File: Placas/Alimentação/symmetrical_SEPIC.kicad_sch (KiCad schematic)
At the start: 10 parts, among them J13 Conn_01x01_Pin, J14 Conn_01x01_Pin, J15 Conn_01x01_Pin, J16 Conn_01x01_Pin, J17 Conn_01x01_Pin

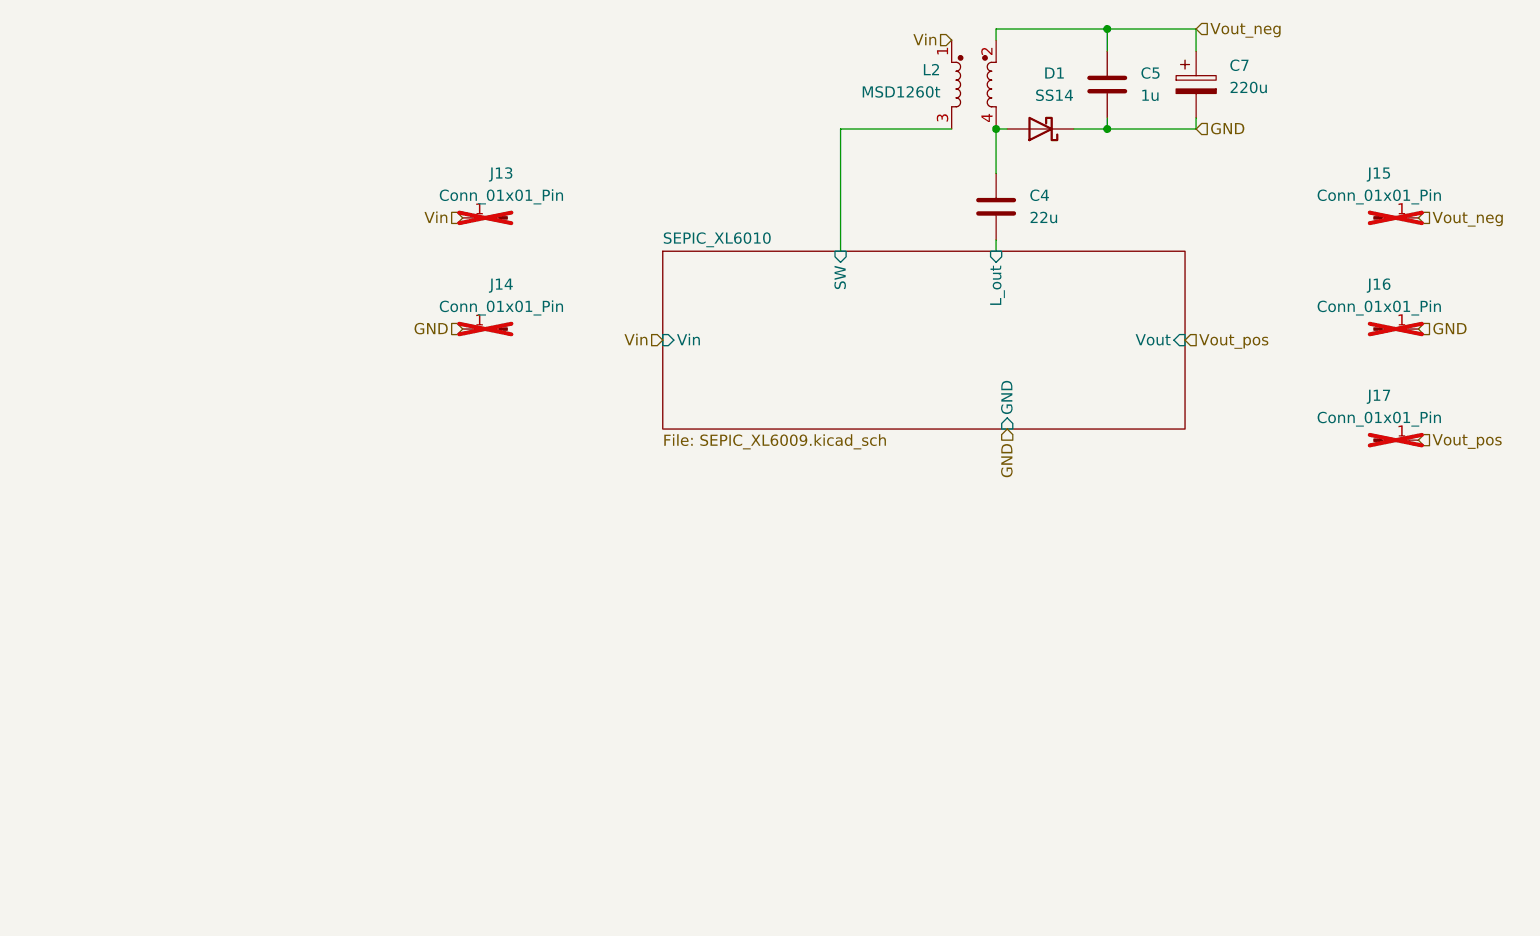
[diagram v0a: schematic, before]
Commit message: Criação dos arquivos em C para o firmware dos dois micros e script em python para salvar aquisição dos dados e envio de comandos
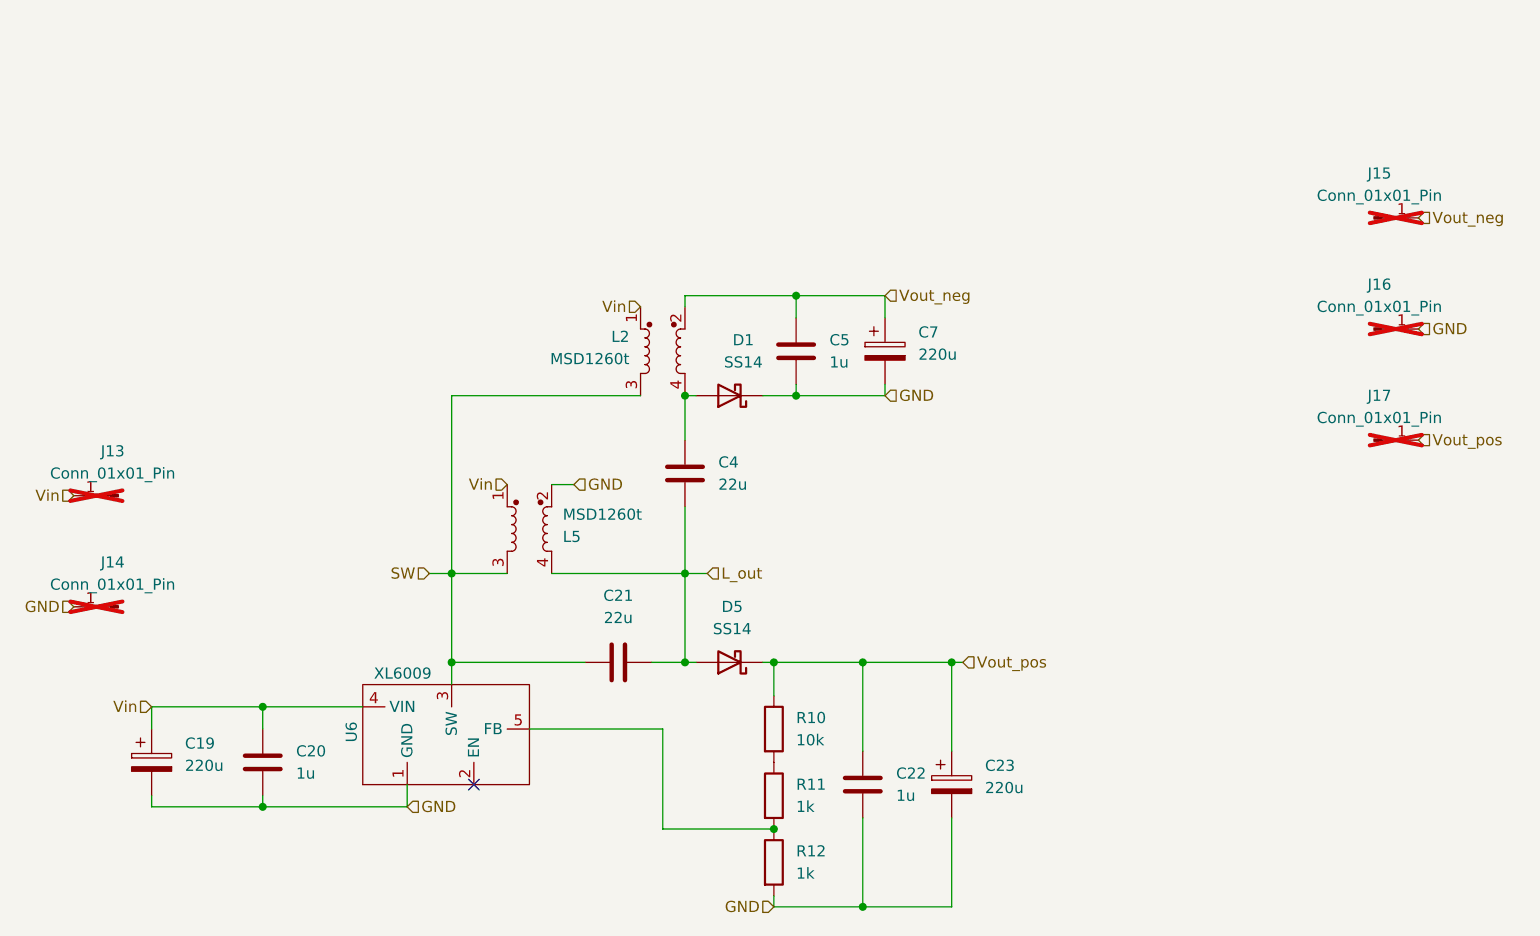
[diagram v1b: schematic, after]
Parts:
- added C19, C23: 220u, Capacitor_SMD:CP_Elec_8x10.5, symbol Device:C_Polarized
- added C20, C22: 1u, Capacitor_SMD:C_0805_2012Metric_Pad1.18x1.45mm_HandSolder, symbol Device:C
- added C21: 22u, Capacitor_SMD:C_0805_2012Metric_Pad1.18x1.45mm_HandSolder, symbol Device:C
- added D5: SS14, Diode_SMD:D_SMA_Handsoldering, symbol Device:D_Schottky
- added L5: MSD1260t, Coupled_inductors:Msd1260t, symbol Device:L_Coupled_1324
- added R10: 10k, Resistor_SMD:R_0805_2012Metric_Pad1.20x1.40mm_HandSolder, symbol Device:R
- added R11, R12: 1k, Resistor_SMD:R_0805_2012Metric_Pad1.20x1.40mm_HandSolder, symbol Device:R
- added U6: XL6009, Package_TO_SOT_SMD:TO-263-5_TabPin3, symbol Modules:XL6009_IC
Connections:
- net GND: now also C19.2, C20.2, C22.2, C23.2, L5.2, R12.2, U6.1 (GND)
- net Vin: now also C19.1, C20.1, L5.1, U6.4 (VIN)
- net Vout_pos: now also C22.1, C23.1, D5.1 (K), R10.1
- net SEPIC_XL6010/L_out renamed L_out
- net L_out: now also C21.2, D5.2 (A), L5.4
- net SEPIC_XL6010/SW renamed SW
- net SW: now also C21.1, L5.3, U6.3 (SW)
- new net: R10.2, R11.1
- new net: R11.2, R12.1, U6.5 (FB)
- no-connect marks 0 -> 1
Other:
- removed sheet SEPIC_XL6010
- moved on the sheet: C4, C5, C7, D1, J13, J14, L2
